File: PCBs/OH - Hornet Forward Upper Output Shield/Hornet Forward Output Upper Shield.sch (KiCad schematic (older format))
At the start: 36 parts, among them J1 LOWER 12V IN, J10 I2C, J11 5V IN, J12 STARBOARD FORMATION, J13 PORT SIDE LIGHTS, J14 PORT FORMATION, J15 ANALOG, J16 Address Select 0, J17 Address Select 1, J18 NEXTION ANA, J19 STARBOARD SIDE LIGHTS, J2 RIGHT OUTPUT DIST, J3 LEFT SERVO, J4 RIGHT_SERVO, J5 LOWER 5V IN, J6 UPPER 5V OUT, J7 NEXTION, J8 7219 OUT, J9 PIXEL LEDS, P1 Power, P2 Analog, P3 Analog, P4 Digital, P5 PWM, P6 PWM, P7 Communication, Q1 IRF1405PBF, Q2 IRF1405PBF, Q3 IRF1405PBF

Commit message: pcb
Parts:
- removed J10: I2C, PT_Library_v001:Molex_1x04_P2.54mm_Vertical, symbol Connector:Conn_01x04_Female
- removed J9: PIXEL LEDS, PT_Library_v001:Molex_1x08_P2.54mm_Vertical, symbol Connector:Conn_01x08_Female
- added Q4, Q5: IRF1405PBF, Mosft:International_Rectifier-PG-TO220-3-02_2008-904-MFG, symbol Hornet-Forward-Output-Upper-Shield-rescue:IRF1405PBF-Mosfet
- added R6, R7: 10, PT_Library_v001:PT_R_Axial_DIN0204_L3.6mm_D1.6mm_P2.54mm_Vertical, symbol Device:R_US
- J12: value STARBOARD FORMATION -> RIGHT FORM
- J14: value PORT FORMATION -> LEFT FORM
- Q1, Q2, Q3: symbol Mosfet:IRF1405PBF -> Hornet-Forward-Output-Upper-Shield-rescue:IRF1405PBF-Mosfet
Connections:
- net labels added: BACKLIGHT_NEG, FLOOD_LIGHTS_NEG, NAV_LIGHT
- net labels removed: APU_MAG, BP_STEP_COIL_A, BP_STEP_COIL_B, BP_STEP_COIL_C, BP_STEP_COIL_D, CA_STEP_COIL_A, CA_STEP_COIL_B, CA_STEP_COIL_C, CA_STEP_COIL_D, LED_CHAIN_1, LED_CHAIN_2, LED_CHAIN_3, LED_CHAIN_4, LED_CHAIN_5, LED_CHAIN_6, R_ALT_STEP_COIL_A, R_ALT_STEP_COIL_B, R_ALT_STEP_COIL_C, R_ALT_STEP_COIL_D
- no-connect marks 28 -> 27

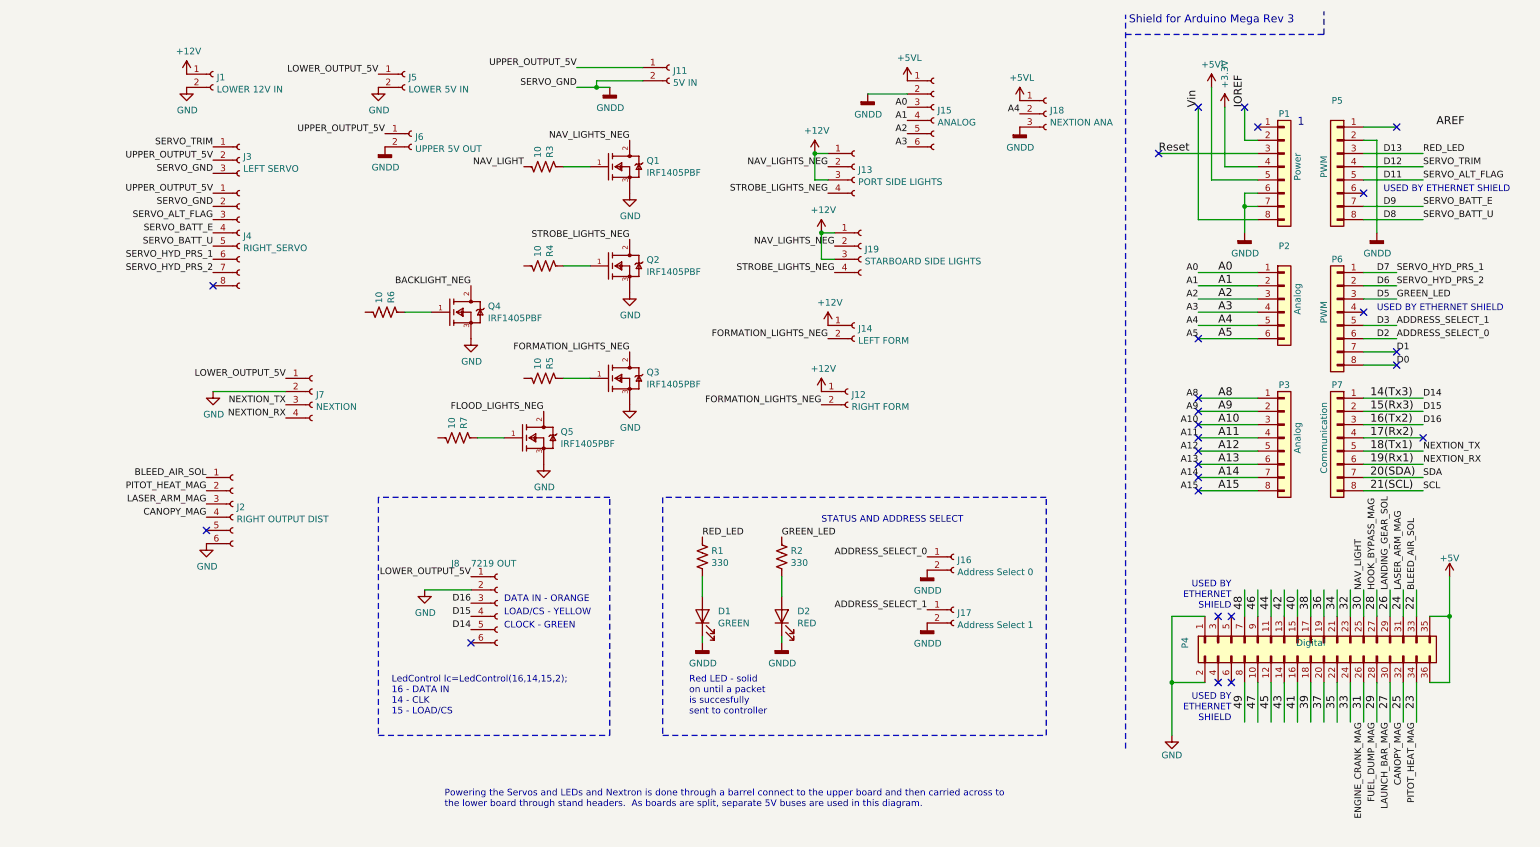
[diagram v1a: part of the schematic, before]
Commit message: Forward upper output PCB
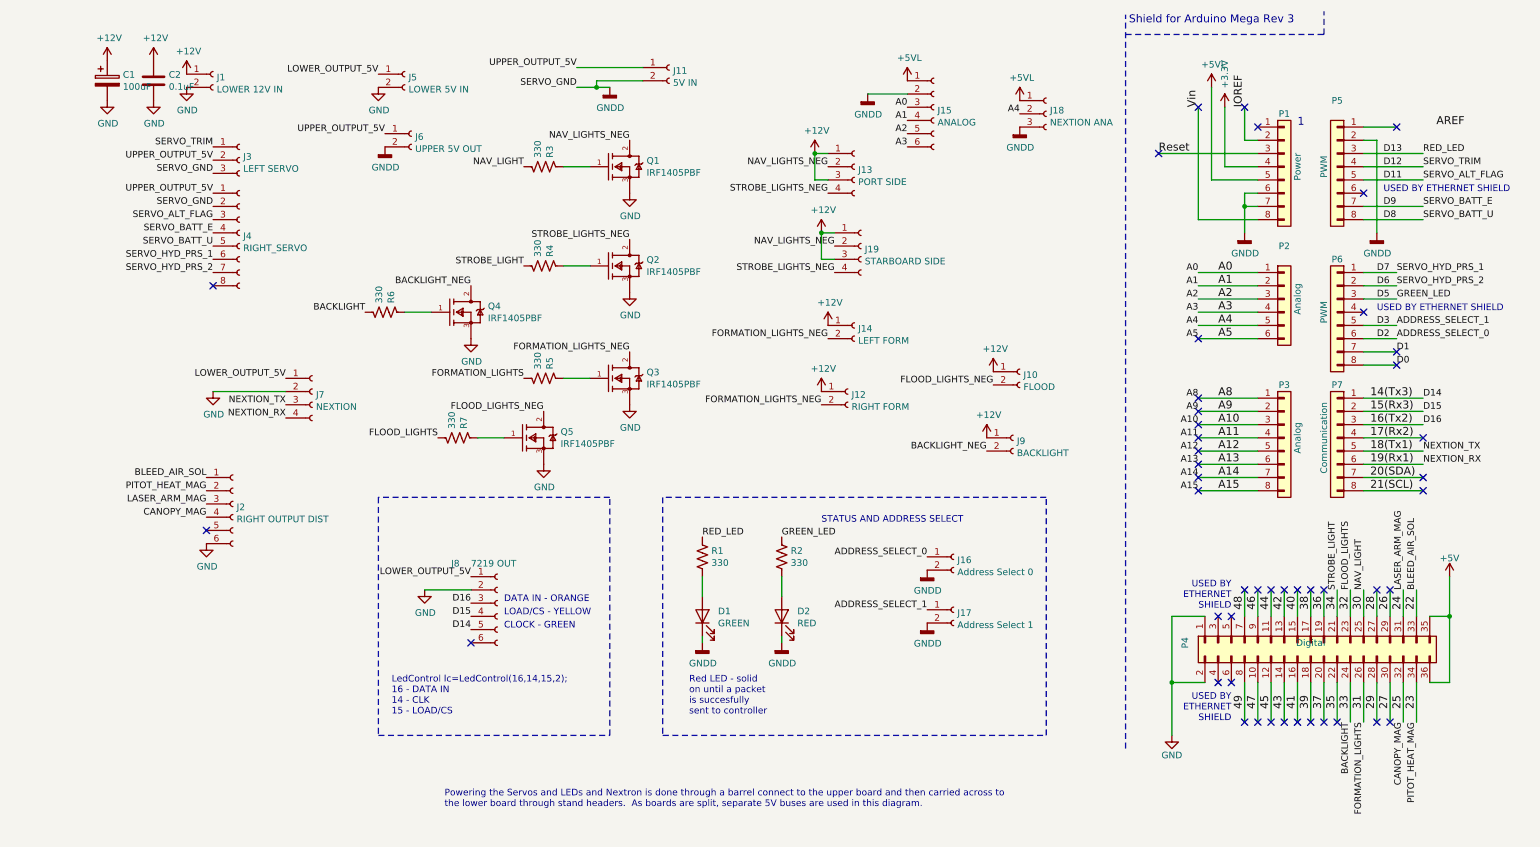
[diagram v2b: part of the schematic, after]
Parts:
- added C1: 100uF, Capacitor_THT:CP_Radial_D5.0mm_P2.50mm, symbol Device:CP
- added C2: 0.1uF, Capacitor_THT:C_Disc_D4.3mm_W1.9mm_P5.00mm, symbol Device:C
- added J10: FLOOD, PT_Library_v001:Molex_1x02_P2.54mm_Vertical, symbol Connector:Conn_01x02_Female
- added J9: BACKLIGHT, PT_Library_v001:Molex_1x02_P2.54mm_Vertical, symbol Connector:Conn_01x02_Female
- J13: value PORT SIDE LIGHTS -> PORT SIDE
- J19: value STARBOARD SIDE LIGHTS -> STARBOARD SIDE
- R3, R4, R5, R6, R7: value 10 -> 330
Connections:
- net labels added: BACKLIGHT, FLOOD_LIGHTS, FORMATION_LIGHTS, STROBE_LIGHT
- net labels removed: ENGINE_CRANK_MAG, FUEL_DUMP_MAG, HOOK_BYPASS_MAG, LANDING_GEAR_SOL, LAUNCH_BAR_MAG, SCL, SDA
- no-connect marks 27 -> 48
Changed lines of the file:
@@
 Text Notes 9150 5000 2    50   ~ 0
 USED BY\nETHERNET\nSHIELD
-Text Label 10350 4850 1    50   ~ 0
-LANDING_GEAR_SOL
-Text Label 10350 5850 3    50   ~ 0
-LAUNCH_BAR_MAG
-Text Label 10250 4850 1    50   ~ 0
-HOOK_BYPASS_MAG
-Text Label 10250 5850 3    50   ~ 0
-FUEL_DUMP_MAG
-Text Label 10150 5850 3    50   ~ 0
-ENGINE_CRANK_MAG
 Text Label 1450 1500 2    50   ~ 0
 SERVO_TRIM
@@
 	1    0    0    -1
 $EndComp
-Text Label 10600 4100 0    50   ~ 0
-SCL
-Text Label 10600 4000 0    50   ~ 0
-SDA
 Text Label 2000 3450 2    50   ~ 0
 NEXTION_TX
@@
 P 3950 1650
 F 0 "R3" H 4018 1696 50  0000 L CNN
-F 1 "10" H 4018 1605 50  0000 L CNN
+F 1 "330" H 4018 1605 50  0000 L CNN
 F 2 "PT_Library_v001:PT_R_Axial_DIN0204_L3.6mm_D1.6mm_P2.54mm_Vertical" V 3990 1640 50  0001 C CNN
 F 3 "~" H 3950 1650 50  0001 C CNN
@@
 P 6300 1650
 F 0 "J13" H 6328 1626 50  0000 L CNN
-F 1 "PORT SIDE LIGHTS" H 6328 1535 50  0000 L CNN
+F 1 "PORT SIDE" H 6328 1535 50  0000 L CNN
 F 2 "PT_Library_v001:Molex_1x04_P2.54mm_Vertical" H 6300 1650 50  0001 C CNN
 F 3 "~" H 6300 1650 50  0001 C CNN
@@
 P 3950 2400
 F 0 "R4" H 4018 2446 50  0000 L CNN
-F 1 "10" H 4018 2355 50  0000 L CNN
+F 1 "330" H 4018 2355 50  0000 L CNN
 F 2 "PT_Library_v001:PT_R_Axial_DIN0204_L3.6mm_D1.6mm_P2.54mm_Vertical" V 3990 2390 50  0001 C CNN
 F 3 "~" H 3950 2400 50  0001 C CNN
@@
 P 3950 3250
 F 0 "R5" H 4018 3296 50  0000 L CNN
-F 1 "10" H 4018 3205 50  0000 L CNN
+F 1 "330" H 4018 3205 50  0000 L CNN
 F 2 "PT_Library_v001:PT_R_Axial_DIN0204_L3.6mm_D1.6mm_P2.54mm_Vertical" V 3990 3240 50  0001 C CNN
 F 3 "~" H 3950 3250 50  0001 C CNN
@@
 P 6350 2250
 F 0 "J19" H 6378 2226 50  0000 L CNN
-F 1 "STARBOARD SIDE LIGHTS" H 6378 2135 50  0000 L CNN
+F 1 "STARBOARD SIDE" H 6378 2135 50  0000 L CNN
 F 2 "PT_Library_v001:Molex_1x04_P2.54mm_Vertical" H 6350 2250 50  0001 C CNN
 F 3 "~" H 6350 2250 50  0001 C CNN
@@
 P 3300 3700
 F 0 "R7" H 3368 3746 50  0000 L CNN
-F 1 "10" H 3368 3655 50  0000 L CNN
+F 1 "330" H 3368 3655 50  0000 L CNN
 F 2 "PT_Library_v001:PT_R_Axial_DIN0204_L3.6mm_D1.6mm_P2.54mm_Vertical" V 3340 3690 50  0001 C CNN
 F 3 "~" H 3300 3700 50  0001 C CNN
@@
 P 2750 2750
 F 0 "R6" H 2818 2796 50  0000 L CNN
-F 1 "10" H 2818 2705 50  0000 L CNN
+F 1 "330" H 2818 2705 50  0000 L CNN
 F 2 "PT_Library_v001:PT_R_Axial_DIN0204_L3.6mm_D1.6mm_P2.54mm_Vertical" V 2790 2740 50  0001 C CNN
 F 3 "~" H 2750 2750 50  0001 C CNN
@@
 Text Label 10150 4850 1    50   ~ 0
 NAV_LIGHT
+Text Label 3150 3700 2    50   ~ 0
+FLOOD_LIGHTS
+Text Label 10050 4850 1    50   ~ 0
+FLOOD_LIGHTS
+Text Label 2600 2750 2    50   ~ 0
+BACKLIGHT
+Text Label 10050 5850 3    50   ~ 0
+BACKLIGHT
+Text Label 3800 2400 2    50   ~ 0
+STROBE_LIGHT
+Text Label 9950 4850 1    50   ~ 0
+STROBE_LIGHT
+$Comp
+L Connector:Conn_01x02_Female J10
+U 1 1 624459AE
+P 7550 3200
+F 0 "J10" H 7578 3176 50  0000 L CNN
+F 1 "FLOOD" H 7578 3085 50  0000 L CNN
+F 2 "PT_Library_v001:Molex_1x02_P2.54mm_Vertical" H 7550 3200 50  0001 C CNN
+F 3 "~" H 7550 3200 50  0001 C CNN
+	1    7550 3200
+	1    0    0    -1
+$EndComp
+$Comp
+L power:+12V #PWR0110
+U 1 1 624459B8
+P 7350 3200
+F 0 "#PWR0110" H 7350 3050 50  0001 C CNN
+F 1 "+12V" H 7365 3373 50  0000 C CNN
+F 2 "" H 7350 3200 50  0001 C CNN
+F 3 "" H 7350 3200 50  0001 C CNN
+	1    7350 3200
+	1    0    0    -1
+$EndComp
+Text Label 7350 3300 2    50   ~ 0
+FLOOD_LIGHTS_NEG
+$Comp
+L Connector:Conn_01x02_Female J9
+U 1 1 624459C3
+P 7500 3700
+F 0 "J9" H 7528 3676 50  0000 L CNN
+F 1 "BACKLIGHT" H 7528 3585 50  0000 L CNN
+F 2 "PT_Library_v001:Molex_1x02_P2.54mm_Vertical" H 7500 3700 50  0001 C CNN
+F 3 "~" H 7500 3700 50  0001 C CNN
+	1    7500 3700
+	1    0    0    -1
+$EndComp
+$Comp
+L power:+12V #PWR0111
+U 1 1 624459CD
+P 7300 3700
+F 0 "#PWR0111" H 7300 3550 50  0001 C CNN
+F 1 "+12V" H 7315 3873 50  0000 C CNN
+F 2 "" H 7300 3700 50  0001 C CNN
+F 3 "" H 7300 3700 50  0001 C CNN
+	1    7300 3700
+	1    0    0    -1
+$EndComp
+Text Label 7300 3800 2    50   ~ 0
+BACKLIGHT_NEG
+NoConn ~ 9850 4850
+NoConn ~ 9750 4850
+NoConn ~ 9650 4850
+NoConn ~ 9550 4850
+NoConn ~ 9450 4850
+NoConn ~ 9350 4850
+NoConn ~ 9250 4850
+NoConn ~ 9250 5850
+NoConn ~ 9350 5850
+NoConn ~ 9450 5850
+NoConn ~ 9550 5850
+NoConn ~ 9650 5850
+NoConn ~ 9750 5850
+NoConn ~ 9850 5850
+NoConn ~ 9950 5850
+NoConn ~ 10250 4850
+NoConn ~ 10350 5850
+NoConn ~ 10250 5850
+NoConn ~ 10350 4850
+NoConn ~ 10600 4000
+NoConn ~ 10600 4100
+Text Label 3800 3250 2    50   ~ 0
+FORMATION_LIGHTS
+Text Label 10150 5850 3    50   ~ 0
+FORMATION_LIGHTS
+$Comp
+L Device:C C2
+U 1 1 624FD5F5
+P 1000 1000
+F 0 "C2" H 1115 1046 50  0000 L CNN
+F 1 "0.1uF" H 1115 955 50  0000 L CNN
+F 2 "Capacitor_THT:C_Disc_D4.3mm_W1.9mm_P5.00mm" H 1038 850 50  0001 C CNN
+F 3 "~" H 1000 1000 50  0001 C CNN
+	1    1000 1000
+	1    0    0    -1
+$EndComp
+$Comp
+L Device:CP C1
+U 1 1 624FE41F
+P 650 1000
+F 0 "C1" H 768 1046 50  0000 L CNN
+F 1 "100uF" H 768 955 50  0000 L CNN
+F 2 "Capacitor_THT:CP_Radial_D5.0mm_P2.50mm" H 688 850 50  0001 C CNN
+F 3 "~" H 650 1000 50  0001 C CNN
+	1    650  1000
+	1    0    0    -1
+$EndComp
+$Comp
+L power:GND #PWR0112
+U 1 1 624FF265
+P 1000 1150
+F 0 "#PWR0112" H 1000 900 50  0001 C CNN
+F 1 "GND" H 1005 977 50  0000 C CNN
+F 2 "" H 1000 1150 50  0001 C CNN
+F 3 "" H 1000 1150 50  0001 C CNN
+	1    1000 1150
+	1    0    0    -1
+$EndComp
+$Comp
+L power:GND #PWR0113
+U 1 1 624FFC3F
+P 650 1150
+F 0 "#PWR0113" H 650 900 50  0001 C CNN
+F 1 "GND" H 655 977 50  0000 C CNN
+F 2 "" H 650 1150 50  0001 C CNN
+F 3 "" H 650 1150 50  0001 C CNN
+	1    650  1150
+	1    0    0    -1
+$EndComp
+$Comp
+L power:+12V #PWR0114
+U 1 1 625018E0
+P 650 850
+F 0 "#PWR0114" H 650 700 50  0001 C CNN
+F 1 "+12V" H 665 1023 50  0000 C CNN
+F 2 "" H 650 850 50  0001 C CNN
+F 3 "" H 650 850 50  0001 C CNN
+	1    650  850
+	1    0    0    -1
+$EndComp
+$Comp
+L power:+12V #PWR0115
+U 1 1 62502A8D
+P 1000 850
+F 0 "#PWR0115" H 1000 700 50  0001 C CNN
+F 1 "+12V" H 1015 1023 50  0000 C CNN
+F 2 "" H 1000 850 50  0001 C CNN
+F 3 "" H 1000 850 50  0001 C CNN
+	1    1000 850
+	1    0    0    -1
+$EndComp
 $EndSCHEMATC

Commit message: mosfet update
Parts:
- added R10, R11, R12, R8, R9: 10K, PT_Library_v001:PT_R_Axial_DIN0204_L3.6mm_D1.6mm_P2.54mm_Vertical, symbol Device:R_US
- Q1, Q2, Q3, Q4, Q5: footprint Mosft:International_Rectifier-PG-TO220-3-02_2008-904-MFG -> Package_TO_SOT_THT:TO-220-3_Vertical
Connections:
- net GND: now also R10.1, R11.1, R12.1, R8.1, R9.1
- net at Q5.1 (G), R7.1: now also R9.2
- net at Q3.1 (G), R5.1: now also R12.2
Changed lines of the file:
@@
 F 0 "Q1" H 4728 1696 50  0000 L CNN
 F 1 "IRF1405PBF" H 4728 1605 50  0000 L CNN
-F 2 "Mosft:International_Rectifier-PG-TO220-3-02_2008-904-MFG" H 4200 2150 50  0001 L CNN
+F 2 "Package_TO_SOT_THT:TO-220-3_Vertical" H 4200 2150 50  0001 L CNN
 F 3 "https://www.infineon.com/dgdl/irf1405pbf.pdf?fileId=5546d462533600a4015355db084a18bb" H 4200 2250 50  0001 L CNN
 F 4 "No" H 4200 2350 50  0001 L CNN "automotive"
@@
 F 0 "Q2" H 4728 2446 50  0000 L CNN
 F 1 "IRF1405PBF" H 4728 2355 50  0000 L CNN
-F 2 "Mosft:International_Rectifier-PG-TO220-3-02_2008-904-MFG" H 4200 2900 50  0001 L CNN
+F 2 "Package_TO_SOT_THT:TO-220-3_Vertical" H 4200 2900 50  0001 L CNN
 F 3 "https://www.infineon.com/dgdl/irf1405pbf.pdf?fileId=5546d462533600a4015355db084a18bb" H 4200 3000 50  0001 L CNN
 F 4 "No" H 4200 3100 50  0001 L CNN "automotive"
@@
 F 0 "Q3" H 4728 3296 50  0000 L CNN
 F 1 "IRF1405PBF" H 4728 3205 50  0000 L CNN
-F 2 "Mosft:International_Rectifier-PG-TO220-3-02_2008-904-MFG" H 4200 3750 50  0001 L CNN
+F 2 "Package_TO_SOT_THT:TO-220-3_Vertical" H 4200 3750 50  0001 L CNN
 F 3 "https://www.infineon.com/dgdl/irf1405pbf.pdf?fileId=5546d462533600a4015355db084a18bb" H 4200 3850 50  0001 L CNN
 F 4 "No" H 4200 3950 50  0001 L CNN "automotive"
@@
 $EndComp
 Wire Wire Line
-	4300 3250 4100 3250
+	4300 3250 4250 3250
 Text Label 4600 3050 2    50   ~ 0
 FORMATION_LIGHTS_NEG
@@
 F 0 "Q5" H 4078 3746 50  0000 L CNN
 F 1 "IRF1405PBF" H 4078 3655 50  0000 L CNN
-F 2 "Mosft:International_Rectifier-PG-TO220-3-02_2008-904-MFG" H 3550 4200 50  0001 L CNN
+F 2 "Package_TO_SOT_THT:TO-220-3_Vertical" H 3550 4200 50  0001 L CNN
 F 3 "https://www.infineon.com/dgdl/irf1405pbf.pdf?fileId=5546d462533600a4015355db084a18bb" H 3550 4300 50  0001 L CNN
 F 4 "No" H 3550 4400 50  0001 L CNN "automotive"
@@
 $EndComp
 Wire Wire Line
-	3650 3700 3450 3700
+	3650 3700 3550 3700
 Text Label 3950 3500 2    50   ~ 0
 FLOOD_LIGHTS_NEG
@@
 F 0 "Q4" H 3528 2796 50  0000 L CNN
 F 1 "IRF1405PBF" H 3528 2705 50  0000 L CNN
-F 2 "Mosft:International_Rectifier-PG-TO220-3-02_2008-904-MFG" H 3000 3250 50  0001 L CNN
+F 2 "Package_TO_SOT_THT:TO-220-3_Vertical" H 3000 3250 50  0001 L CNN
 F 3 "https://www.infineon.com/dgdl/irf1405pbf.pdf?fileId=5546d462533600a4015355db084a18bb" H 3000 3350 50  0001 L CNN
 F 4 "No" H 3000 3450 50  0001 L CNN "automotive"
@@
 	1    0    0    -1
 $EndComp
+$Comp
+L Device:R_US R9
+U 1 1 62463EEC
+P 3550 3850
+F 0 "R9" H 3618 3896 50  0000 L CNN
+F 1 "10K" H 3618 3805 50  0000 L CNN
+F 2 "PT_Library_v001:PT_R_Axial_DIN0204_L3.6mm_D1.6mm_P2.54mm_Vertical" V 3590 3840 50  0001 C CNN
+F 3 "~" H 3550 3850 50  0001 C CNN
+	1    3550 3850
+	1    0    0    1
+$EndComp
+Connection ~ 3550 3700
+Wire Wire Line
+	3550 3700 3450 3700
+$Comp
+L power:GND #PWR024
+U 1 1 624654D1
+P 3550 4000
+F 0 "#PWR024" H 3550 3750 50  0001 C CNN
+F 1 "GND" H 3555 3827 50  0000 C CNN
+F 2 "" H 3550 4000 50  0001 C CNN
+F 3 "" H 3550 4000 50  0001 C CNN
+	1    3550 4000
+	1    0    0    -1
+$EndComp
+$Comp
+L Device:R_US R12
+U 1 1 62466E4F
+P 4250 3400
+F 0 "R12" H 4318 3446 50  0000 L CNN
+F 1 "10K" H 4318 3355 50  0000 L CNN
+F 2 "PT_Library_v001:PT_R_Axial_DIN0204_L3.6mm_D1.6mm_P2.54mm_Vertical" V 4290 3390 50  0001 C CNN
+F 3 "~" H 4250 3400 50  0001 C CNN
+	1    4250 3400
+	1    0    0    1
+$EndComp
+$Comp
+L power:GND #PWR027
+U 1 1 62466E59
+P 4250 3550
+F 0 "#PWR027" H 4250 3300 50  0001 C CNN
+F 1 "GND" H 4255 3377 50  0000 C CNN
+F 2 "" H 4250 3550 50  0001 C CNN
+F 3 "" H 4250 3550 50  0001 C CNN
+	1    4250 3550
+	1    0    0    -1
+$EndComp
+Connection ~ 4250 3250
+Wire Wire Line
+	4250 3250 4100 3250
+$Comp
+L Device:R_US R8
+U 1 1 6246F48A
+P 3000 2900
+F 0 "R8" H 3068 2946 50  0000 L CNN
+F 1 "10K" H 3068 2855 50  0000 L CNN
+F 2 "PT_Library_v001:PT_R_Axial_DIN0204_L3.6mm_D1.6mm_P2.54mm_Vertical" V 3040 2890 50  0001 C CNN
+F 3 "~" H 3000 2900 50  0001 C CNN
+	1    3000 2900
+	1    0    0    1
+$EndComp
+$Comp
+L power:GND #PWR08
+U 1 1 6246F490
+P 3000 3050
+F 0 "#PWR08" H 3000 2800 50  0001 C CNN
+F 1 "GND" H 3005 2877 50  0000 C CNN
+F 2 "" H 3000 3050 50  0001 C CNN
+F 3 "" H 3000 3050 50  0001 C CNN
+	1    3000 3050
+	1    0    0    -1
+$EndComp
+$Comp
+L Device:R_US R10
+U 1 1 62473EF9
+P 4200 2550
+F 0 "R10" H 4268 2596 50  0000 L CNN
+F 1 "10K" H 4268 2505 50  0000 L CNN
+F 2 "PT_Library_v001:PT_R_Axial_DIN0204_L3.6mm_D1.6mm_P2.54mm_Vertical" V 4240 2540 50  0001 C CNN
+F 3 "~" H 4200 2550 50  0001 C CNN
+	1    4200 2550
+	1    0    0    1
+$EndComp
+$Comp
+L power:GND #PWR025
+U 1 1 62473EFF
+P 4200 2700
+F 0 "#PWR025" H 4200 2450 50  0001 C CNN
+F 1 "GND" H 4205 2527 50  0000 C CNN
+F 2 "" H 4200 2700 50  0001 C CNN
+F 3 "" H 4200 2700 50  0001 C CNN
+	1    4200 2700
+	1    0    0    -1
+$EndComp
+$Comp
+L Device:R_US R11
+U 1 1 62479292
+P 4250 1800
+F 0 "R11" H 4318 1846 50  0000 L CNN
+F 1 "10K" H 4318 1755 50  0000 L CNN
+F 2 "PT_Library_v001:PT_R_Axial_DIN0204_L3.6mm_D1.6mm_P2.54mm_Vertical" V 4290 1790 50  0001 C CNN
+F 3 "~" H 4250 1800 50  0001 C CNN
+	1    4250 1800
+	1    0    0    1
+$EndComp
+$Comp
+L power:GND #PWR026
+U 1 1 62479298
+P 4250 1950
+F 0 "#PWR026" H 4250 1700 50  0001 C CNN
+F 1 "GND" H 4255 1777 50  0000 C CNN
+F 2 "" H 4250 1950 50  0001 C CNN
+F 3 "" H 4250 1950 50  0001 C CNN
+	1    4250 1950
+	1    0    0    -1
+$EndComp

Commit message: PCB
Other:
- note added: "SILSCREEN TO AS USED"
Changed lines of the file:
@@
 	1    0    0    -1
 $EndComp
+Text Notes 3400 7000 0    118  ~ 0
+SILSCREEN TO AS USED
 $EndSCHEMATC

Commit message: PCB
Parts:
- removed J16: Address Select 0, Connector_PinHeader_2.54mm:PinHeader_1x02_P2.54mm_Vertical, symbol Connector:Conn_01x02_Female
- removed J17: Address Select 1, Connector_PinHeader_2.54mm:PinHeader_1x02_P2.54mm_Vertical, symbol Connector:Conn_01x02_Female
- removed J2: RIGHT OUTPUT DIST, PT_Library_v001:Molex_1x06_P2.54mm_Vertical, symbol Connector:Conn_01x06_Female
- removed J3: LEFT SERVO, PT_Library_v001:Molex_1x03_P2.54mm_Vertical, symbol Connector:Conn_01x03_Female
- removed J4: RIGHT_SERVO, PT_Library_v001:Molex_1x08_P2.54mm_Vertical, symbol Connector:Conn_01x08_Female
- added J2: UPPER 12V IN, PT_Library_v001:Molex_1x02_P2.54mm_Vertical, symbol Connector:Conn_01x02_Female
- added J3: MAP, PT_Library_v001:Molex_1x02_P2.54mm_Vertical, symbol Connector:Conn_01x02_Female
- added J4: LOWER 12V OUT, PT_Library_v001:Molex_1x02_P2.54mm_Vertical, symbol Connector:Conn_01x02_Female
- added Q6: IRF1405PBF, Package_TO_SOT_THT:TO-220-3_Vertical, symbol Hornet-Forward-Output-Upper-Shield-rescue:IRF1405PBF-Mosfet
- added R13: 330, PT_Library_v001:PT_R_Axial_DIN0204_L3.6mm_D1.6mm_P2.54mm_Vertical, symbol Device:R_US
- added R14: 10K, PT_Library_v001:PT_R_Axial_DIN0204_L3.6mm_D1.6mm_P2.54mm_Vertical, symbol Device:R_US
- J15: value ANALOG -> RELAY OUT
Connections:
- net +12V: now also J4.1 (Pin_1); no longer J10.1 (Pin_1), J12.1 (Pin_1), J14.1 (Pin_1)
- net +5VL: no longer J15.1 (Pin_1)
- net 22: now also J15.1 (Pin_1)
- net 23: now also J15.2 (Pin_2)
- net 24: now also J15.3 (Pin_3)
- net 25: now also J15.4 (Pin_4)
- net 30: no longer R3.2
- net 31: no longer R5.2
- net 32: no longer R7.2
- net 33: no longer R6.2
- net 34: no longer R4.2
- net 44: now also R4.2
- net 45: now also R3.2
- net 46: now also R6.2
- net A0: no longer J15.3 (Pin_3)
- net A1: no longer J15.4 (Pin_4)
- net A2: no longer J15.5 (Pin_5)
- net A3: no longer J15.6 (Pin_6)
- net D6: now also R13.2
- net D7: now also R7.2
- net D8: now also R5.2
- net GND: now also J15.6 (Pin_6), J4.2 (Pin_2); no longer Q3.3 (S), Q5.3 (S), R12.1, R9.1
- net GNDD: now also Q3.3 (S), Q5.3 (S), R12.1, R9.1, J2.2 (Pin_2), Q6.3 (S), R14.1; no longer J15.2 (Pin_2)
- net at Q1.1 (G), R3.1: now also R11.2
- net at Q2.1 (G), R4.1: now also R10.2
- net at R8.2: now also Q4.1 (G), R6.1
- net ADDRESS_SELECT_0 renamed D2
- net ADDRESS_SELECT_1 renamed D3
- net BACKLIGHT_NEG: no longer names the net of J9.2 (Pin_2), Q4.2 (D)
- net FLOOD_LIGHTS_NEG: no longer names the net of J10.2 (Pin_2), Q5.2 (D)
- new net: Q6.1 (G), R13.1, R14.2
- new net: J3.2 (Pin_2), Q6.2 (D)
- new net +12VA: J10.1 (Pin_1), J12.1 (Pin_1), J14.1 (Pin_1), J2.1 (Pin_1), J3.1 (Pin_1)
- no-connect marks 48 -> 59
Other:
- note added: "Powering the Servos and LEDs and Nextron is done through a barrel connect to the upper board and then carried across to \nthe lower board through stand headers. As boards are split, separate 5V and 12V buses are used in this diagram."
- note removed: "Powering the Servos and LEDs and Nextron is done through a barrel connect to the upper board and then carried across to \nthe lower board through stand headers. As boards are split, separate 5V buses are used in this diagram."
- note removed: "SILSCREEN TO AS USED"
- moved on the sheet: D1, D2, J10, J11, J12, J13, J14, J18, J19, J5, J6, J7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
